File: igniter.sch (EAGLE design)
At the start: 11 parts, among them X1 Break, X2 IGN1, X3 IGN2

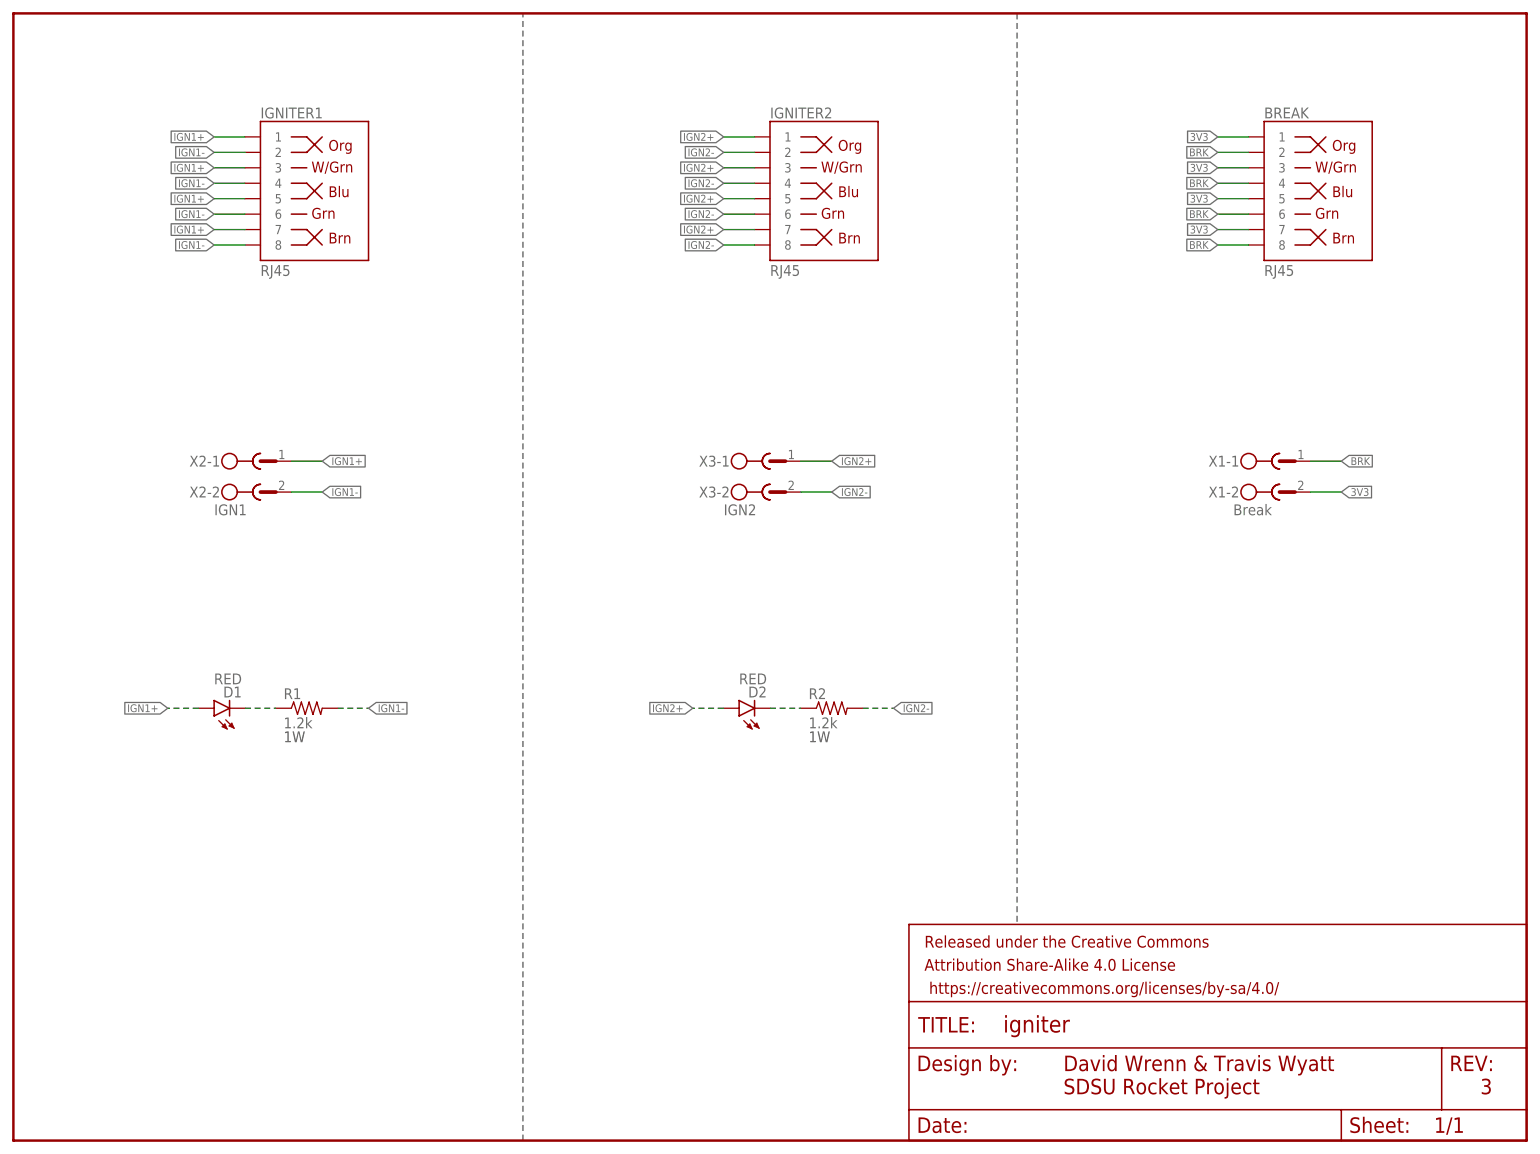
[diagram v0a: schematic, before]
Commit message: Updated to use more efficient LEDs. Decreased SMD resistor size to 0603.
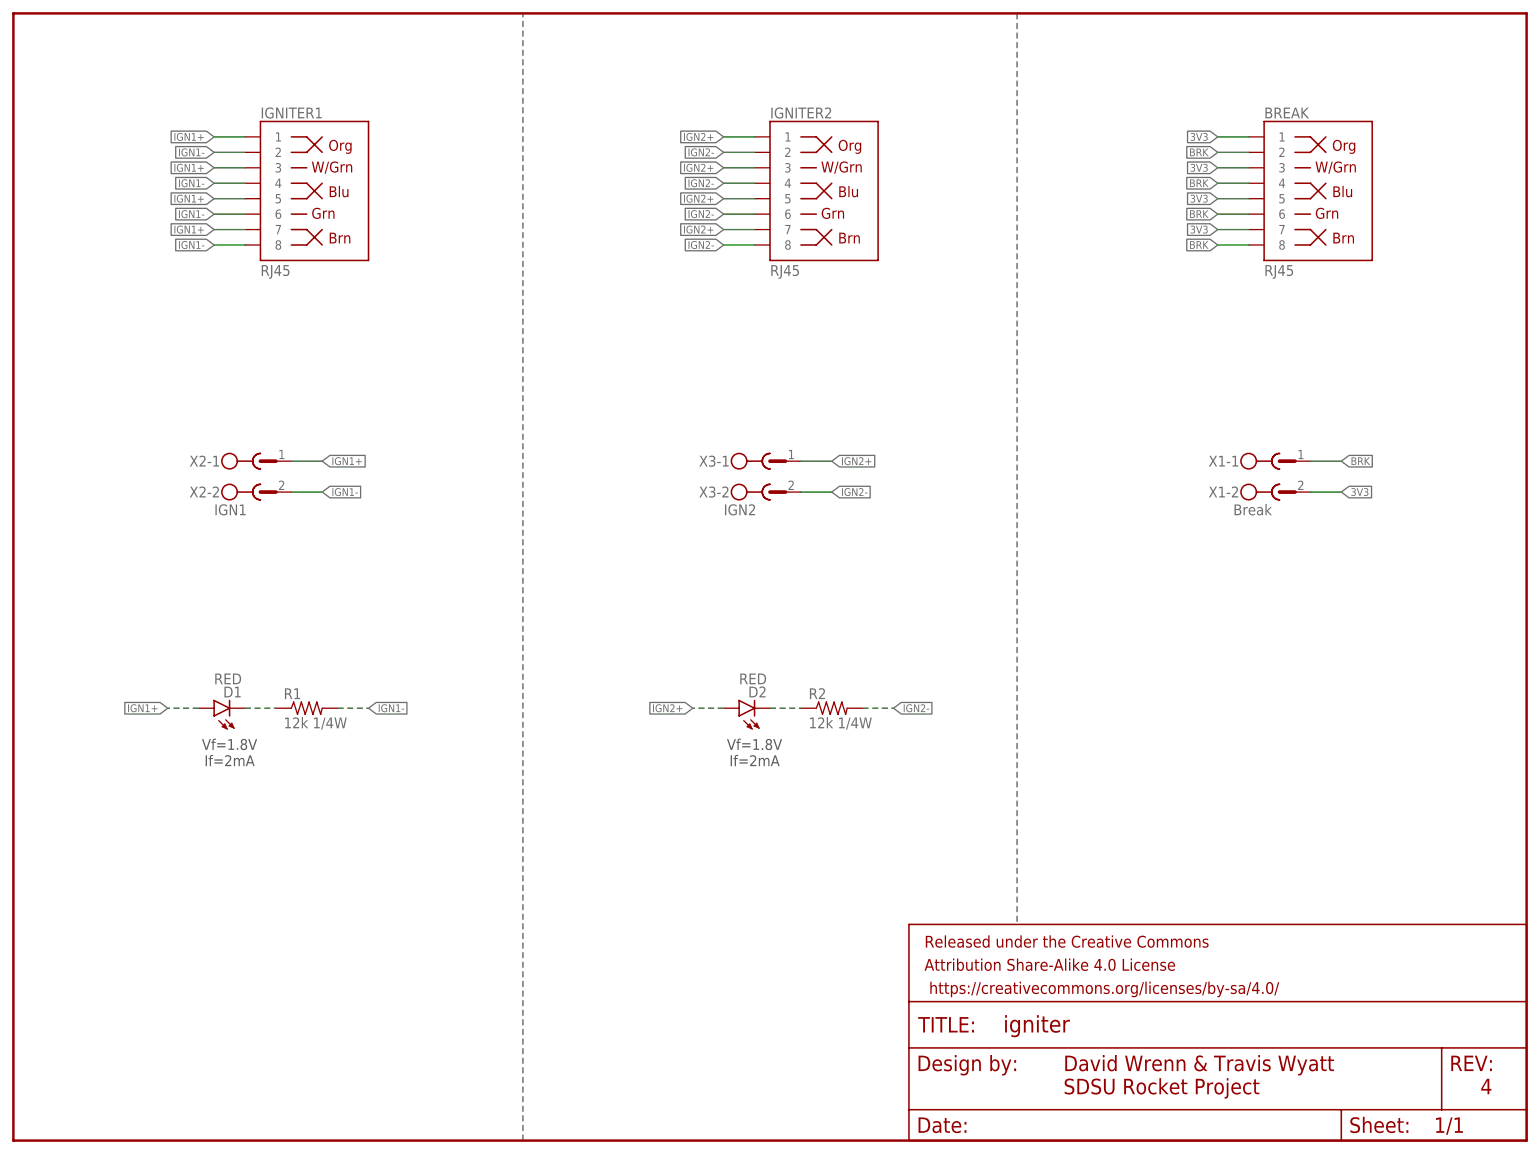
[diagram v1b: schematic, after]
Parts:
- R1, R2: value 1.2k -> 12k 1/4W; device SparkFun-Resistors:RESISTOR2512 -> SparkFun-Resistors:RESISTOR0603-RES
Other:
- note added: "4"
- note added: "Vf=1.8V If=2mA"
- note removed: "1W"
- note removed: "3"
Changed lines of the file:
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@@
 <part name="D1" library="SparkFun-LED" deviceset="LED" device="0603" value="RED"/>
 <part name="FRAME1" library="SparkFun-Aesthetics" deviceset="FRAME-LETTER" device=""/>
-<part name="R1" library="SparkFun-Resistors" deviceset="RESISTOR" device="2512" value="1.2k"/>
+<part name="R1" library="SparkFun-Resistors" deviceset="RESISTOR" device="0603-RES" value="12k 1/4W"/>
 <part name="D2" library="SparkFun-LED" deviceset="LED" device="0603" value="RED"/>
-<part name="R2" library="SparkFun-Resistors" deviceset="RESISTOR" device="2512" value="1.2k"/>
+<part name="R2" library="SparkFun-Resistors" deviceset="RESISTOR" device="0603-RES" value="12k 1/4W"/>
 </parts>
 <sheets>
@@
 <wire x1="83.82" y1="0" x2="83.82" y2="185.42" width="0.2032" layer="97" style="longdash"/>
 <wire x1="165.1" y1="185.42" x2="165.1" y2="35.56" width="0.2032" layer="97" style="longdash"/>
-<text x="44.45" y="65.532" size="1.778" layer="97">1W</text>
-<text x="130.81" y="65.532" size="1.778" layer="97">1W</text>
-<text x="241.3" y="7.62" size="2.54" layer="94">3</text>
+<text x="241.3" y="7.62" size="2.54" layer="94">4</text>
 <text x="172.72" y="12.7" size="2.54" layer="94" align="center-left">David Wrenn &amp; Travis Wyatt</text>
 <text x="172.72" y="8.89" size="2.54" layer="94" align="center-left">SDSU Rocket Project</text>
+<text x="35.56" y="66.04" size="1.778" layer="97" align="top-center">Vf=1.8V
+If=2mA</text>
+<text x="121.92" y="66.04" size="1.778" layer="97" align="top-center">Vf=1.8V
+If=2mA</text>
 </plain>
 <instances>
@@
 </schematic>
 </drawing>
+<compatibility>
+<note version="6.3" minversion="6.2.2" severity="warning">
+Since Version 6.2.2 text objects can contain more than one line,
+which will not be processed correctly with this version.
+</note>
+</compatibility>
 </eagle>
